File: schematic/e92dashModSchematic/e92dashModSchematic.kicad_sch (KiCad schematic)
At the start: 2 parts, among them U1 ESP32-DevKitC, U2 Ender3 LCD

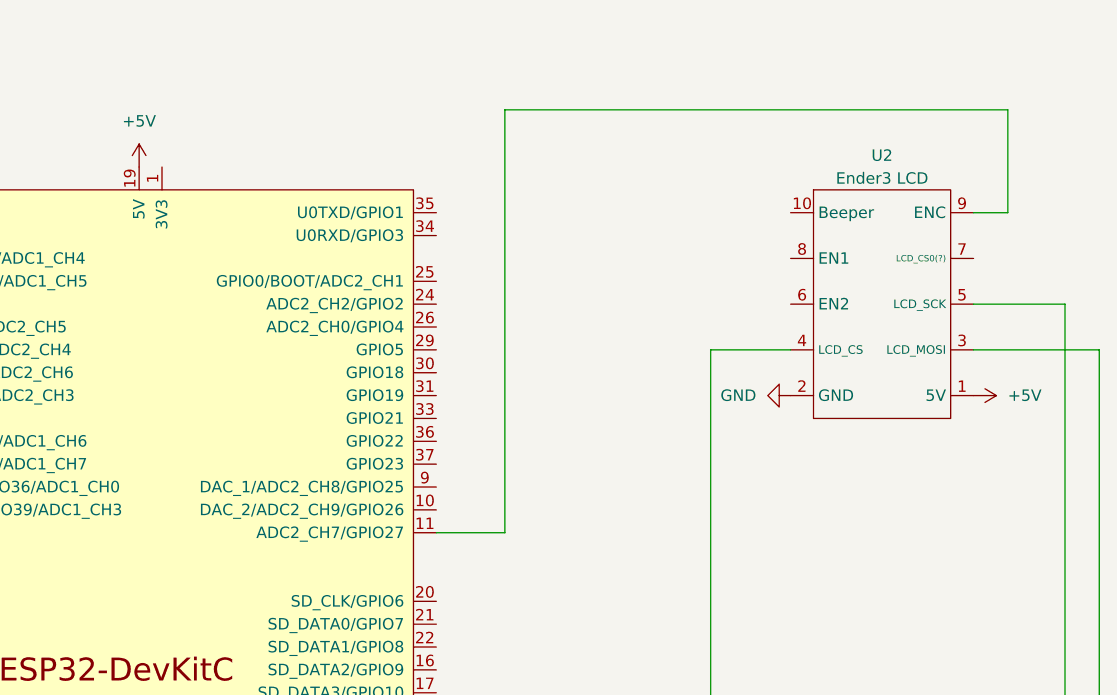
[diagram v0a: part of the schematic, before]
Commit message: fix encoder button wiring
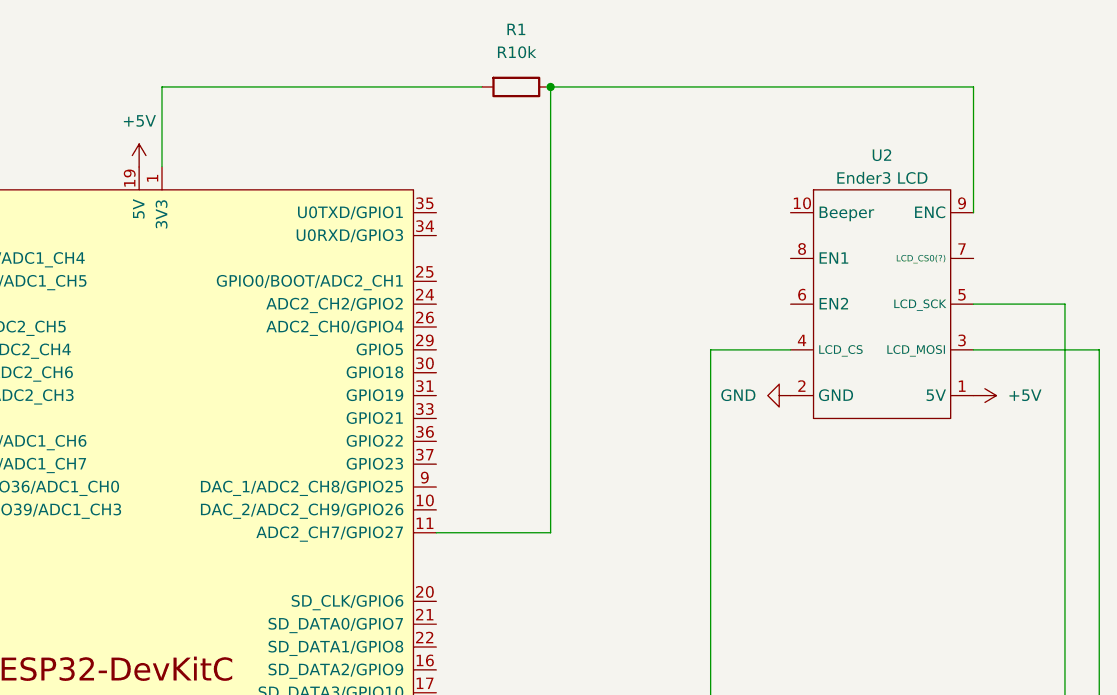
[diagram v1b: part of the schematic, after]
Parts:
- added R1: R10k, symbol Device:R
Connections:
- net at U1.1 (3V3): now also R1.2
- net at U1.11 (ADC2_CH7/GPIO27), U2.9 (ENC): now also R1.1
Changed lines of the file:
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@@
 	(generator_version "8.0")
 	(paper "A4")
+	(junction
+		(at 120.65 53.34)
+		(diameter 0)
+		(color 0 0 0 0)
+	)
 	(wire
 		(pts
@@
 	(wire
 		(pts
-			(xy 115.57 55.88) (xy 115.57 102.87)
+			(xy 167.64 53.34) (xy 167.64 67.31)
 		)
 		(stroke
@@
 	(wire
 		(pts
+			(xy 120.65 102.87) (xy 120.65 53.34)
+		)
+		(stroke
+			(width 0)
+			(type default)
+		)
+	)
+	(wire
+		(pts
 			(xy 177.8 77.47) (xy 177.8 143.51)
 		)
@@
 	(wire
 		(pts
-			(xy 115.57 102.87) (xy 107.95 102.87)
-		)
-		(stroke
-			(width 0)
-			(type default)
-		)
-	)
-	(wire
-		(pts
 			(xy 177.8 143.51) (xy 33.02 143.51)
 		)
@@
 	(wire
 		(pts
+			(xy 77.47 53.34) (xy 113.03 53.34)
+		)
+		(stroke
+			(width 0)
+			(type default)
+		)
+	)
+	(wire
+		(pts
 			(xy 35.56 85.09) (xy 41.91 85.09)
 		)
@@
 	(wire
 		(pts
-			(xy 171.45 67.31) (xy 167.64 67.31)
-		)
-		(stroke
-			(width 0)
-			(type default)
-		)
-	)
-	(wire
-		(pts
-			(xy 171.45 55.88) (xy 171.45 67.31)
-		)
-		(stroke
-			(width 0)
-			(type default)
-		)
-	)
-	(wire
-		(pts
-			(xy 115.57 55.88) (xy 171.45 55.88)
+			(xy 120.65 53.34) (xy 167.64 53.34)
 		)
 		(stroke
@@
 		(pts
 			(xy 35.56 140.97) (xy 35.56 85.09)
+		)
+		(stroke
+			(width 0)
+			(type default)
+		)
+	)
+	(wire
+		(pts
+			(xy 77.47 62.23) (xy 77.47 53.34)
+		)
+		(stroke
+			(width 0)
+			(type default)
+		)
+	)
+	(wire
+		(pts
+			(xy 107.95 102.87) (xy 120.65 102.87)
 		)
 		(stroke
@@
 					(unit 1)
 				)
+			)
+		)
+	)
+	(symbol
+		(lib_id "Device:R")
+		(at 116.84 53.34 270)
+		(unit 1)
+		(exclude_from_sim no)
+		(in_bom yes)
+		(on_board yes)
+		(dnp no)
+		(fields_autoplaced yes)
+		(property "Reference" "R1"
+			(at 116.84 46.99 90)
+			(effects
+				(font
+					(size 1.27 1.27)
+				)
+			)
+		)
+		(property "Value" "R10k"
+			(at 116.84 49.53 90)
+			(effects
+				(font
+					(size 1.27 1.27)
+				)
+			)
+		)
+		(property "Footprint" ""
+			(at 116.84 51.562 90)
+			(effects
+				(font
+					(size 1.27 1.27)
+				)
+				(hide yes)
+			)
+		)
+		(property "Datasheet" "~"
+			(at 116.84 53.34 0)
+			(effects
+				(font
+					(size 1.27 1.27)
+				)
+				(hide yes)
+			)
+		)
+		(property "Description" "Resistor"
+			(at 116.84 53.34 0)
+			(effects
+				(font
+					(size 1.27 1.27)
+				)
+				(hide yes)
+			)
+		)
+		(pin "2"
+		)
+		(pin "1"
+		)
+		(instances
+			(project ""
+				(path "/1715f863-40a5-41cf-b4fd-78de2582a0a4"
+					(reference "R1")
+					(unit 1)
+				)

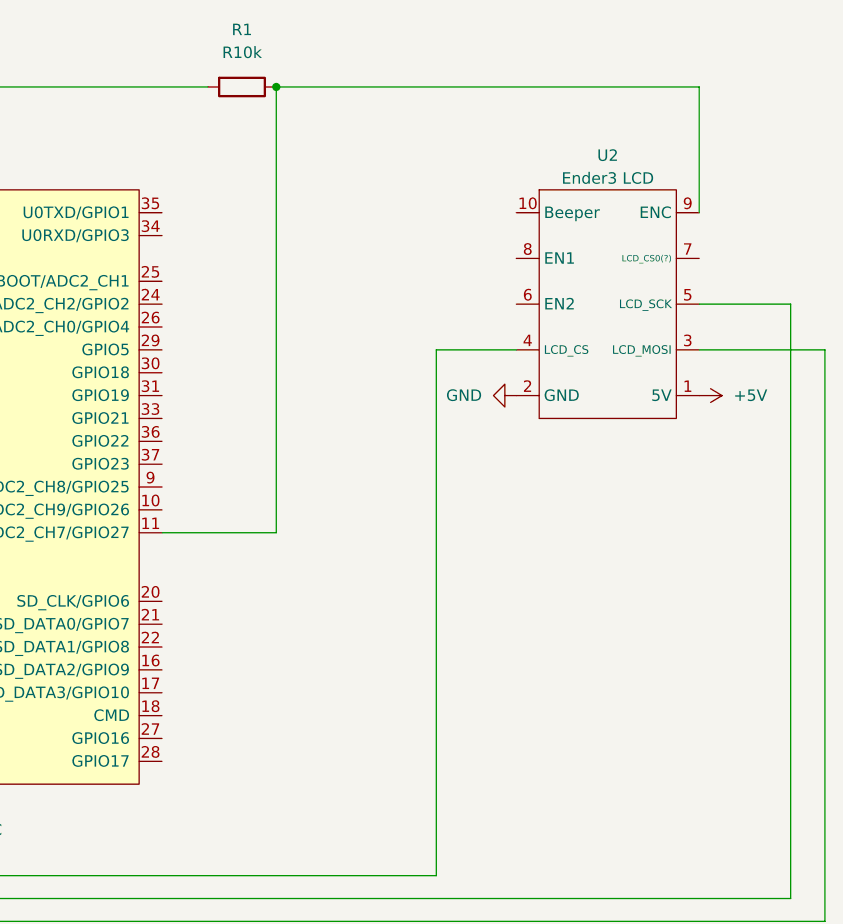
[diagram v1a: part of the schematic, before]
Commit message: added LCD on/off functionality, added .gitignore
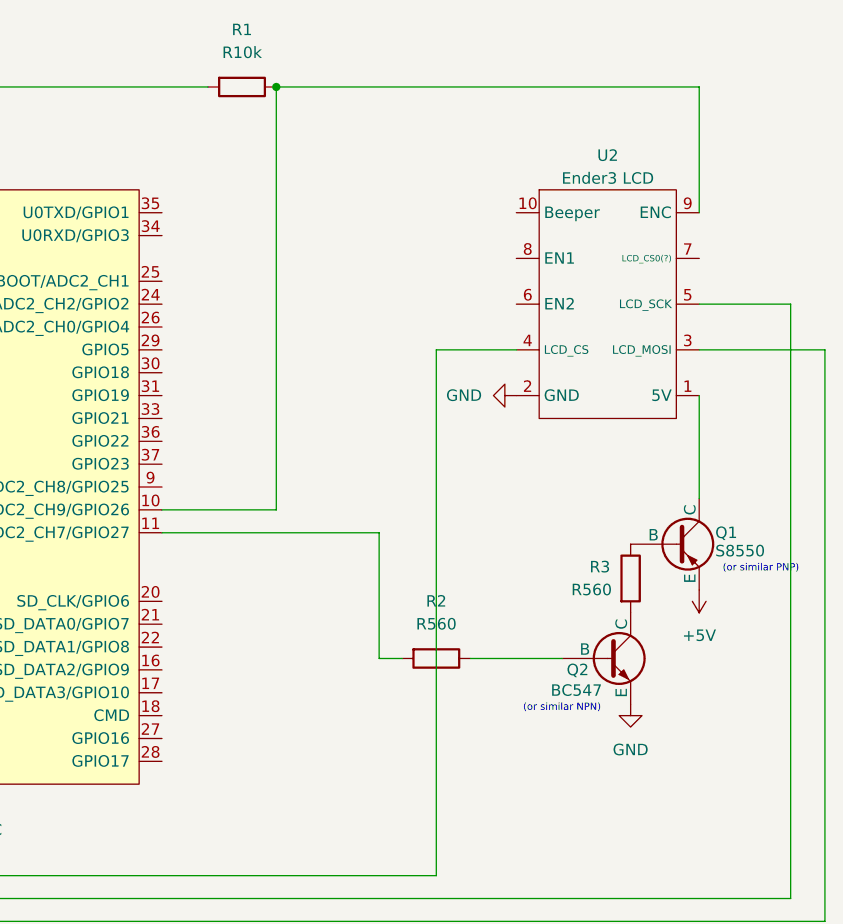
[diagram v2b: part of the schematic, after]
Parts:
- added Q1: S8550, Package_TO_SOT_THT:TO-92_Inline, symbol Transistor_BJT:S8550
- added Q2: BC547, Package_TO_SOT_THT:TO-92_Inline, symbol Transistor_BJT:BC547
- added R2, R3: R560, symbol Device:R
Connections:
- net +5V: now also Q1.1 (E); no longer U2.1 (5V)
- net GND: now also Q2.3 (E)
- net at U1.10 (DAC_2/ADC2_CH9/GPIO26): now also R1.1, U2.9 (ENC)
- new net: Q1.2 (B), R3.1
- new net: Q1.3 (C), U2.1 (5V)
- new net: R2.2, U1.11 (ADC2_CH7/GPIO27)
- new net: Q2.1 (C), R3.2
- new net: Q2.2 (B), R2.1
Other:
- note added: "(or similar NPN)"
- note added: "(or similar PNP)"

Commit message: updated CAN functionality (should work now) and extended README
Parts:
- added U3: MCP2515 (symbolic), Package_SO:SOIC-18W_7.5x11.6mm_P1.27mm, symbol Interface_CAN_LIN:MCP2515-xSO
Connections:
- net GND: now also U3.9 (VSS)
- net at U1.29 (GPIO5): now also U3.16 (~{CS})
- net at U1.30 (GPIO18): now also U3.13 (SCK)
- net at U1.31 (GPIO19): now also U3.15 (SO)
- net at U1.37 (GPIO23): now also U3.14 (SI)
- new net +3.3V: U3.18 (VDD)
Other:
- moved on the sheet: Q1, Q2, R1, R2, R3, U1, U2

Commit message: added more detail on the LCD pinout
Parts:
- U2: value Ender3 LCD -> Ender 3 LCD (EXP3)
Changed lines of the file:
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@@
 			)
 		)
-		(property "Value" "Ender3 LCD"
+		(property "Value" "Ender 3 LCD (EXP3)"
 			(at 156.21 35.56 0)
 			(effects
@@
 			)
 		)
-		(property "Description" ""
+		(property "Description" "Connector pinout of the Ender 3 LCD (rightmost connector EXP3, cutout on the left indicated by the black rectangle)"
 			(at 156.21 49.53 0)
 			(effects
